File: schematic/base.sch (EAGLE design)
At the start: 10 parts, among them Q1 BC557, Q2 BC557

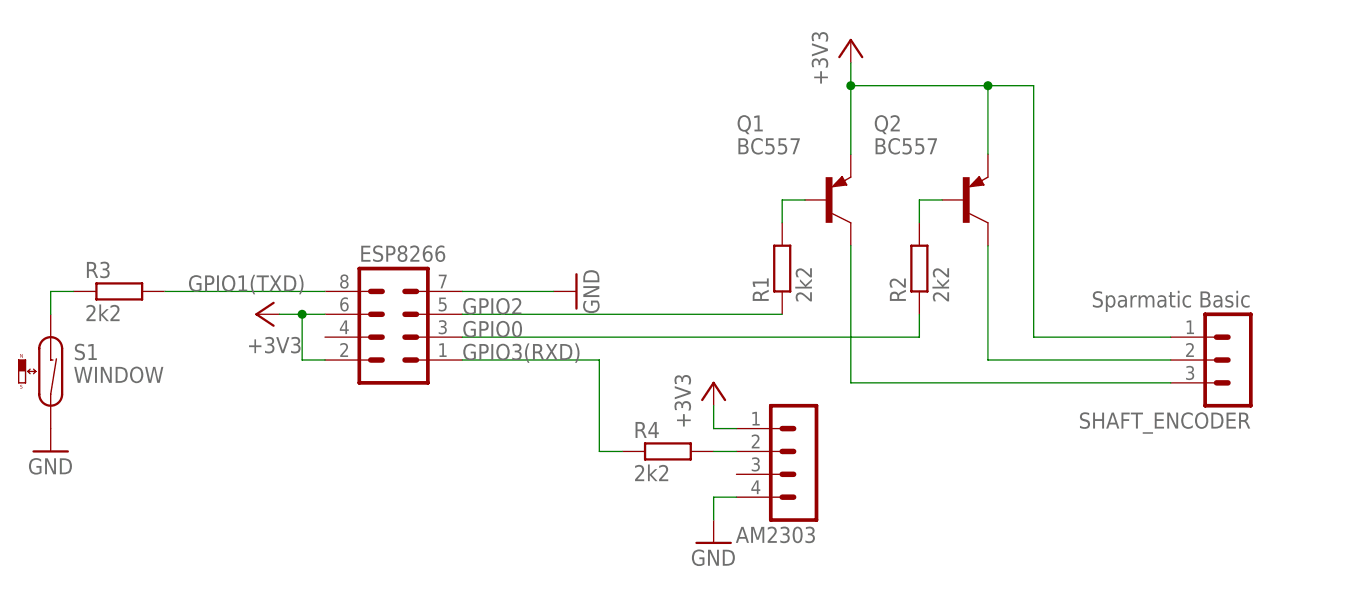
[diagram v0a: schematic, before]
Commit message: Add DHT to sematic
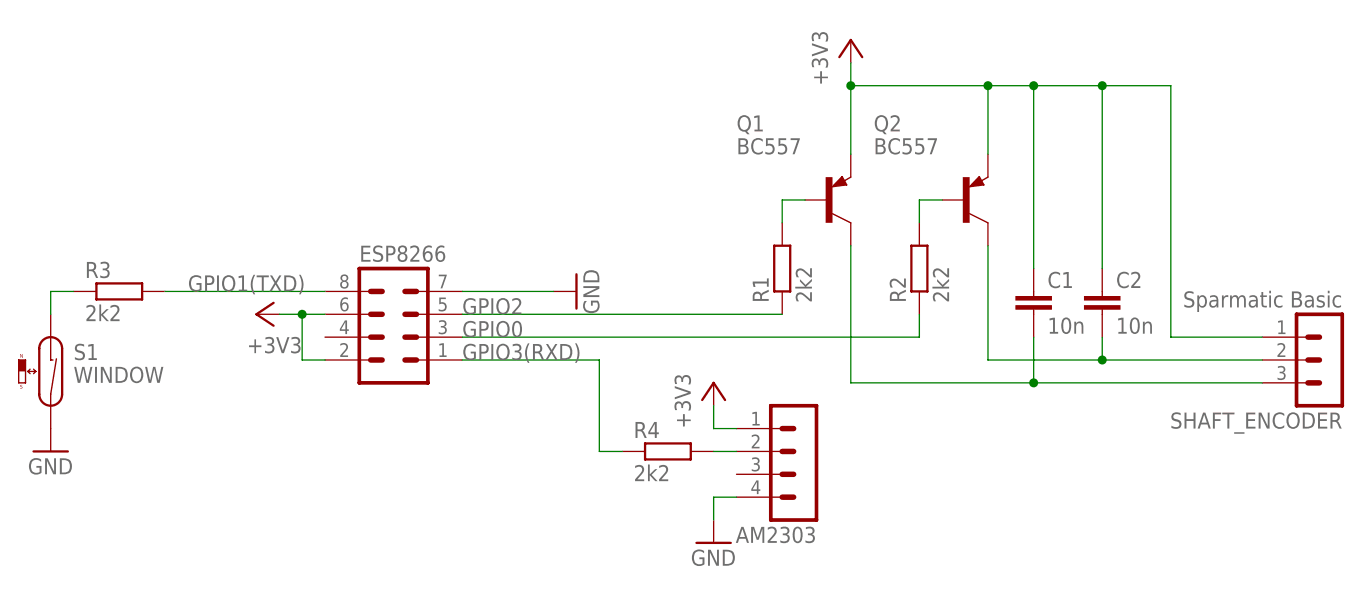
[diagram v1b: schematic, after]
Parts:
- added C1, C2: 10n, rcl:C-EU075-032X103
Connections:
- net +3V3: now also C1.1, C2.1
- net N$4: now also C2.2
- net N$5: now also C1.2
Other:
- moved on the sheet: SHAFT_ENCODER
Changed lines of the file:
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@@
 <part name="GND3" library="supply1" deviceset="GND" device=""/>
 <part name="R4" library="rcl" deviceset="R-EU_" device="0204/7" value="2k2"/>
+<part name="C1" library="rcl" deviceset="C-EU" device="075-032X103" value="10n"/>
+<part name="C2" library="rcl" deviceset="C-EU" device="075-032X103" value="10n"/>
 </parts>
 <sheets>
@@
 <instance part="S1" gate="G$1" x="15.24" y="22.86"/>
 <instance part="GND2" gate="1" x="15.24" y="15.24"/>
-<instance part="SHAFT_ENCODER" gate="G$1" x="147.32" y="25.4" rot="R180"/>
+<instance part="SHAFT_ENCODER" gate="G$1" x="157.48" y="25.4" rot="R180"/>
 <instance part="AM2303" gate="1" x="99.06" y="12.7" rot="R180"/>
 <instance part="+3V3" gate="G$1" x="88.9" y="22.86"/>
 <instance part="GND3" gate="1" x="88.9" y="5.08"/>
 <instance part="R4" gate="G$1" x="83.82" y="15.24"/>
+<instance part="C1" gate="G$1" x="124.46" y="33.02"/>
+<instance part="C2" gate="G$1" x="132.08" y="33.02"/>
 </instances>
 <busses>
@@
 <wire x1="119.38" y1="55.88" x2="119.38" y2="48.26" width="0.1524" layer="91"/>
 <junction x="104.14" y="55.88"/>
-<pinref part="SHAFT_ENCODER" gate="G$1" pin="1"/>
-<wire x1="139.7" y1="27.94" x2="124.46" y2="27.94" width="0.1524" layer="91"/>
-<wire x1="124.46" y1="27.94" x2="124.46" y2="55.88" width="0.1524" layer="91"/>
 <wire x1="124.46" y1="55.88" x2="119.38" y2="55.88" width="0.1524" layer="91"/>
 <junction x="119.38" y="55.88"/>
+<pinref part="C1" gate="G$1" pin="1"/>
+<wire x1="124.46" y1="35.56" x2="124.46" y2="55.88" width="0.1524" layer="91"/>
+<pinref part="C2" gate="G$1" pin="1"/>
+<wire x1="132.08" y1="35.56" x2="132.08" y2="55.88" width="0.1524" layer="91"/>
+<wire x1="132.08" y1="55.88" x2="124.46" y2="55.88" width="0.1524" layer="91"/>
+<junction x="124.46" y="55.88"/>
+<pinref part="SHAFT_ENCODER" gate="G$1" pin="1"/>
+<wire x1="149.86" y1="27.94" x2="139.7" y2="27.94" width="0.1524" layer="91"/>
+<wire x1="139.7" y1="27.94" x2="139.7" y2="55.88" width="0.1524" layer="91"/>
+<wire x1="139.7" y1="55.88" x2="132.08" y2="55.88" width="0.1524" layer="91"/>
+<junction x="132.08" y="55.88"/>
 </segment>
 <segment>
@@
 <wire x1="119.38" y1="38.1" x2="119.38" y2="25.4" width="0.1524" layer="91"/>
 <pinref part="SHAFT_ENCODER" gate="G$1" pin="2"/>
-<wire x1="119.38" y1="25.4" x2="139.7" y2="25.4" width="0.1524" layer="91"/>
+<wire x1="119.38" y1="25.4" x2="132.08" y2="25.4" width="0.1524" layer="91"/>
+<pinref part="C2" gate="G$1" pin="2"/>
+<wire x1="132.08" y1="25.4" x2="149.86" y2="25.4" width="0.1524" layer="91"/>
+<wire x1="132.08" y1="27.94" x2="132.08" y2="25.4" width="0.1524" layer="91"/>
+<junction x="132.08" y="25.4"/>
 </segment>
 </net>
@@
 <pinref part="SHAFT_ENCODER" gate="G$1" pin="3"/>
 <pinref part="Q1" gate="G$1" pin="C"/>
-<wire x1="139.7" y1="22.86" x2="104.14" y2="22.86" width="0.1524" layer="91"/>
+<wire x1="149.86" y1="22.86" x2="124.46" y2="22.86" width="0.1524" layer="91"/>
+<wire x1="124.46" y1="22.86" x2="104.14" y2="22.86" width="0.1524" layer="91"/>
 <wire x1="104.14" y1="22.86" x2="104.14" y2="38.1" width="0.1524" layer="91"/>
+<pinref part="C1" gate="G$1" pin="2"/>
+<wire x1="124.46" y1="27.94" x2="124.46" y2="22.86" width="0.1524" layer="91"/>
+<junction x="124.46" y="22.86"/>
 </segment>
 </net>
